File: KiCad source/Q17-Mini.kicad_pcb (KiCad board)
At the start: 2 copper layers, 95 x 75 mm, 85 parts, among them J1 Input, Q1 FQP3N30, Q10 KSA992, Q11 BS250P, Q12 BD139, Q13 FQP3N30, Q14 IRF9610, Q15 FQA46N15, Q16 FQA36P15, Q2 KSA992, Q3 KSC1845, Q4 FQP3P20, Q5 FQP3P20, Q6 FQP3N30, Q7 KSC1845, Q8 2N7000, Q9 BS250P, U1 OPA1641

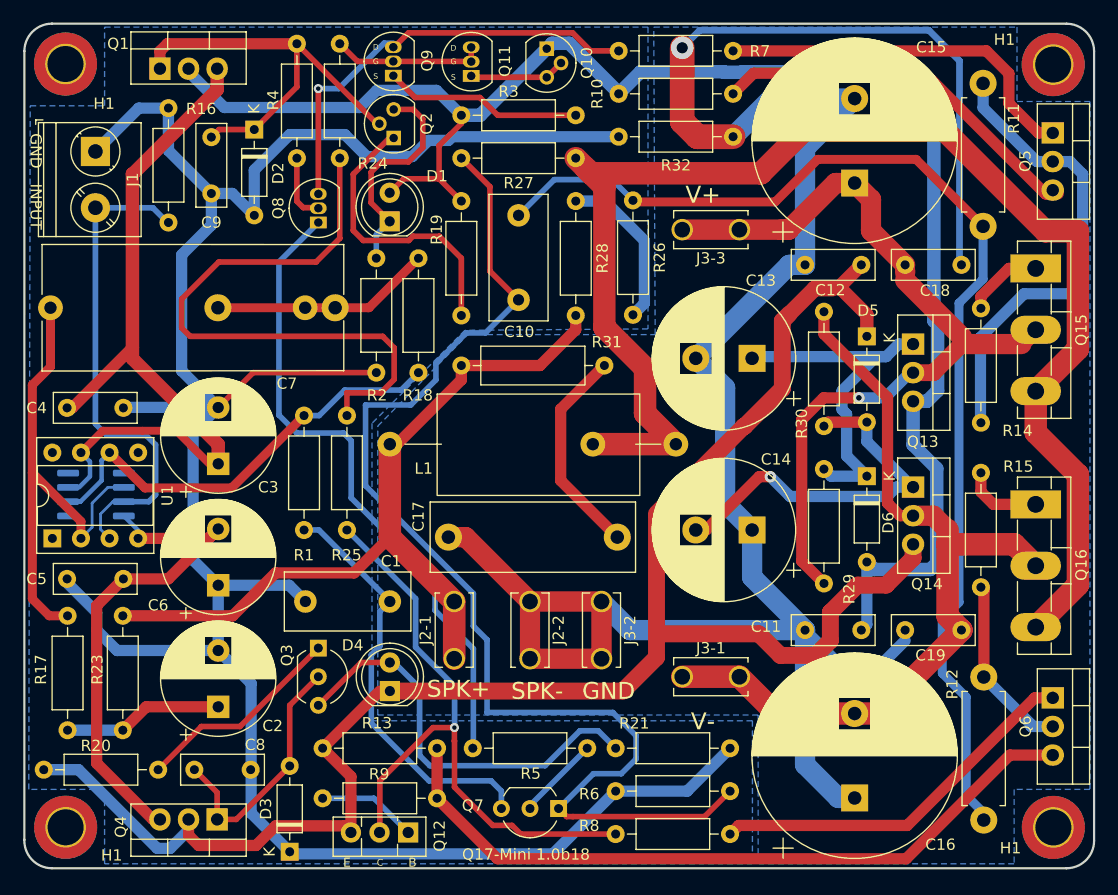
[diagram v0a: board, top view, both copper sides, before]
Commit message: PCB version 1.0b19
More mods on ground plane.
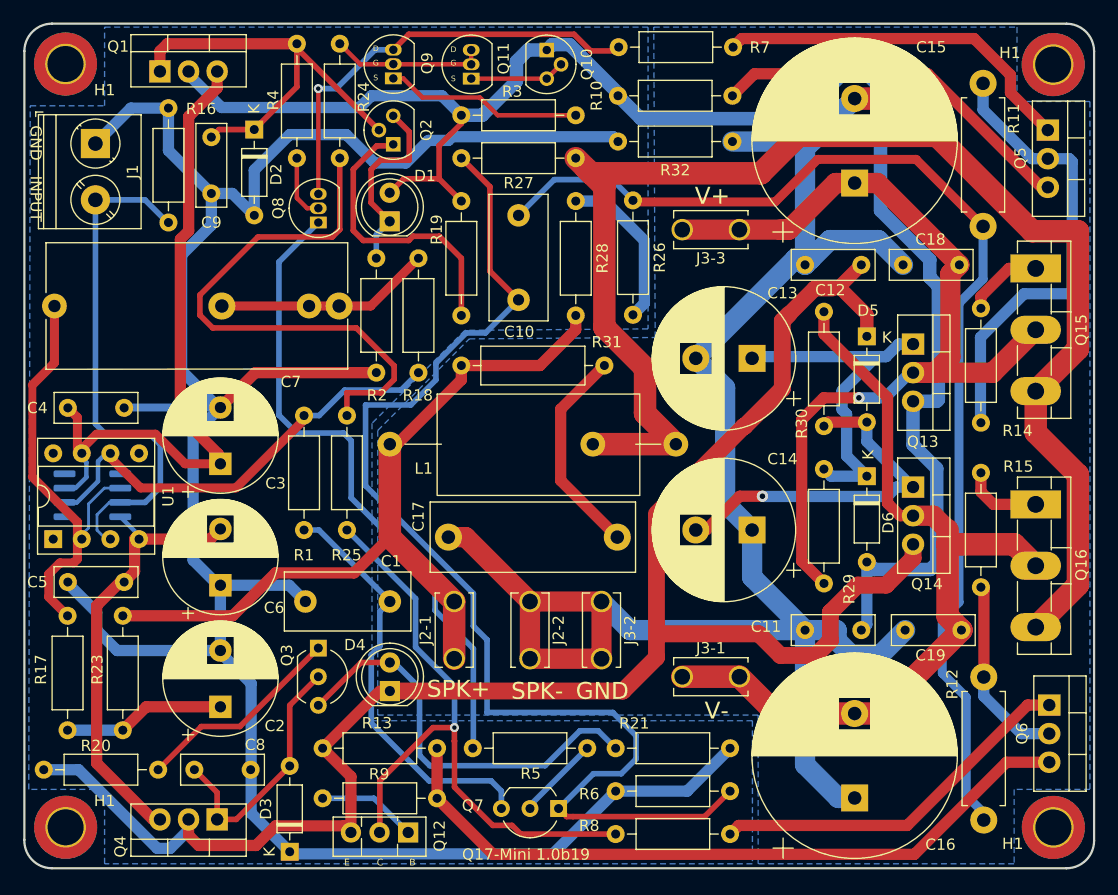
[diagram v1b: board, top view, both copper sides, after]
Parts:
- moved C18 5.19 mm to (177.8, 76.5), turned to 0 degrees
- moved Q6 0.71 mm to (190.8, 115.6)
- moved J1 0.70 mm to (106.1, 65.7)
- moved Q2 0.57 mm to (132.6, 65.8)
- moved Q5 0.51 mm to (190.7, 64.5)
- moved R32 0.43 mm to (152.5, 65.5)
- moved C7 0.38 mm to (102.4, 80.1)
- moved R7 0.33 mm to (152.6, 57.1)
- moved U1 0.32 mm to (105.9, 96.9)
- moved C5 0.29 mm to (103.7, 104.6)
- moved Q1 0.25 mm to (111.9, 59.3)
- moved Q11 0.24 mm to (139.5, 59.9)
- moved Q9 0.24 mm to (132.6, 59.9)
- moved C2 0.19 mm to (117.2, 115.7)
- moved C3 0.19 mm to (117.2, 94.2)
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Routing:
- net GNDPWR: track 207.5 -> 168.3 mm
- net Net-(C3-Pad1): track 67.4 -> 60.3 mm
- net Net-(C15-Pad1): track 75.4 -> 82.4 mm
- net Net-(C5-Pad2): track 45.3 -> 39.7 mm
- net Net-(C7-Pad1): track 44.8 -> 39.4 mm
- net Net-(R24-Pad2): track 55.1 -> 50.0 mm
- net Net-(D1-Pad1): track 19.8 -> 17.3 mm
- net Net-(J1-Pad2): track 43.8 -> 45.6 mm
- net Net-(C14-Pad2): track 33.7 -> 32.3 mm
- net Net-(Q5-Pad3): track 34.1 -> 33.0 mm
- net Net-(Q6-Pad3): track 65.2 -> 64.3 mm
- net Net-(Q6-Pad2): track 16.1 -> 17.0 mm
- net Net-(Q6-Pad1): track 33.8 -> 33.1 mm
- net Net-(C11-Pad2): track 146.6 -> 147.1 mm
- net Net-(Q5-Pad2): track 41.6 -> 41.1 mm
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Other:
- board text added: "Q17-Mini 1.0b19"
- board text added: "QUAD405 Audiophile Tiberiu Vicol PCB Design by Stef PROTO RELEASE 2021"
- board text removed: "2022"
- board text removed: "Q17-Mini 1.0b18"
- board text removed: "QUAD405 Audiophile Tiberiu Vicol PCB Design by Stef PROTO RELEASE"

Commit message: PCB 1.0b20
- New Faston PAD footprint + 3D view.
- Removed old GND track.
- More track optimisation.
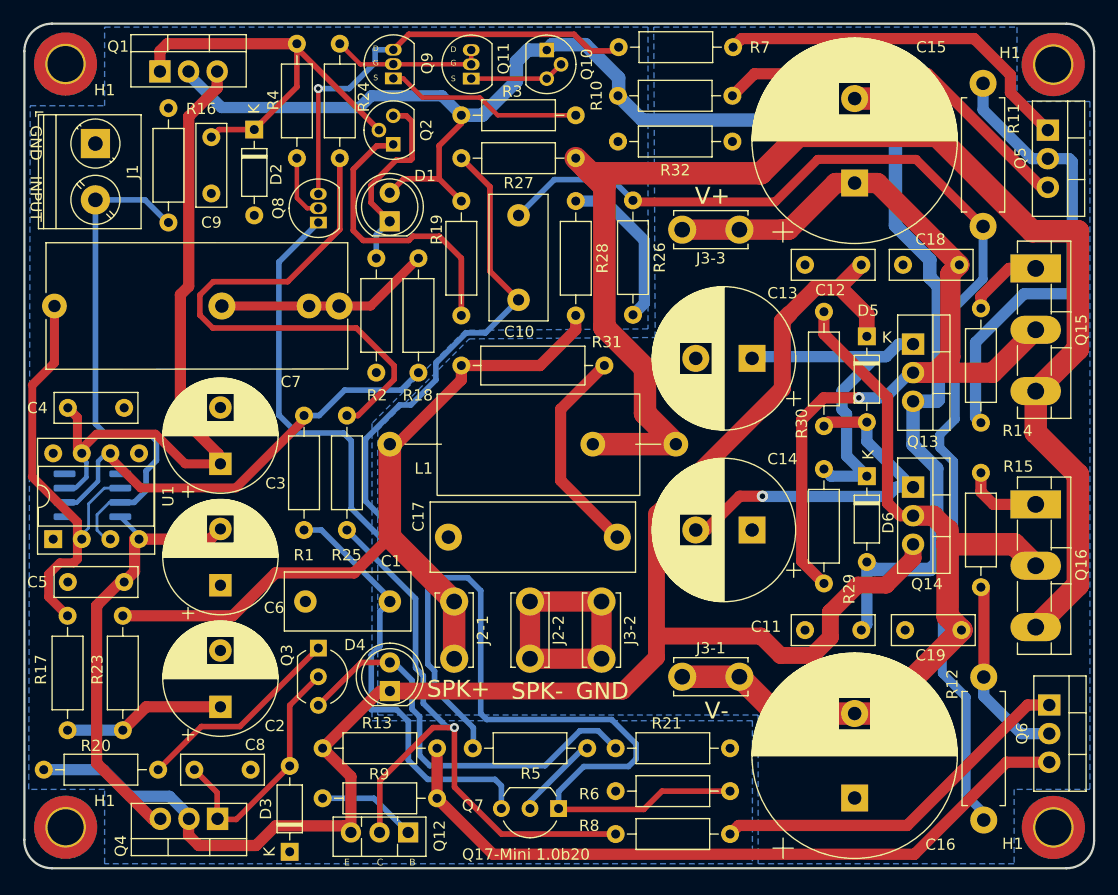
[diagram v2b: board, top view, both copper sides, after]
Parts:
- moved Q4 0.07 mm to (117.0, 125.7)
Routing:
- net GND: track 220.3 -> 0.39 mm
- net GNDPWR: track 168.3 -> 29.2 mm
- net Net-(C11-Pad2): track 147.1 -> 149.7 mm
- net Net-(C1-Pad1): track 37.3 -> 39.0 mm
- net Net-(C12-Pad2): track 152.8 -> 151.5 mm
- net Net-(R24-Pad2): track 50.0 -> 48.8 mm
- net Net-(C10-Pad1): track 103.4 -> 104.4 mm
- net Net-(J1-Pad2): track 45.6 -> 44.7 mm
- net Net-(Q8-Pad3): track 38.6 -> 39.3 mm
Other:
- board text added: "Q17-Mini 1.0b20"
- board text removed: "Q17-Mini 1.0b19"

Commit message: PCB 1.0b21
- New footprint for Silver Mica capacitors.
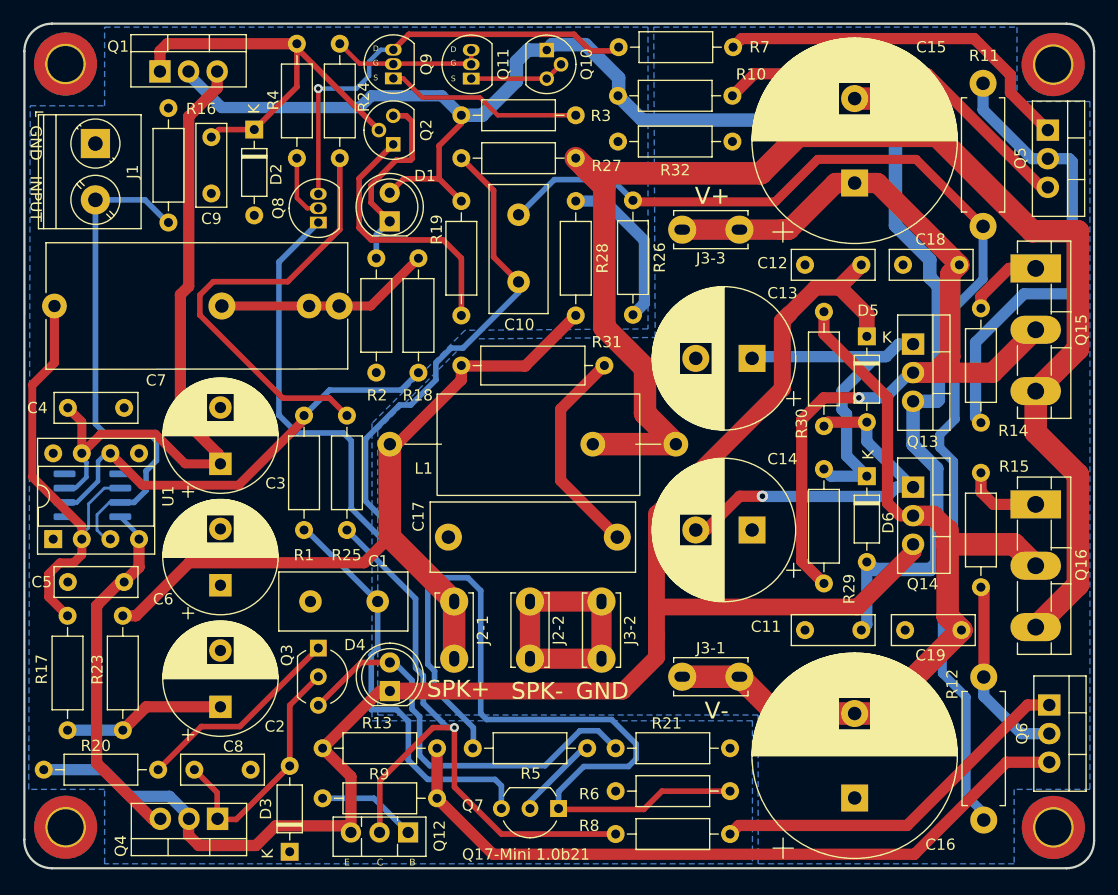
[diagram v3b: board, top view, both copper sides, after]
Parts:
- C1, C10: footprint Capacitor_THT:C_Disc_D11.0mm_W5.0mm_P7.50mm -> Silver_Mica:C_Mica_L11.4mm_W4.3mm_H9.1_P5.9mm
- moved C1 1.14 mm to (131.1, 106.4)
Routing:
- net Net-(R24-Pad2): track 48.8 -> 39.7 mm
- net Net-(C5-Pad2): track 39.7 -> 31.9 mm
- net Net-(C12-Pad2): track 151.5 -> 147.4 mm
- net Net-(Q2-Pad1): track 25.9 -> 23.9 mm
- net Net-(C1-Pad1): track 39.0 -> 37.4 mm
- net Net-(J2-Pad1): track 70.8 -> 70.0 mm
- net Net-(R1-Pad1): track 40.0 -> 39.4 mm
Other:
- board text added: "Q17-Mini 1.0b21"
- board text removed: "Q17-Mini 1.0b20"

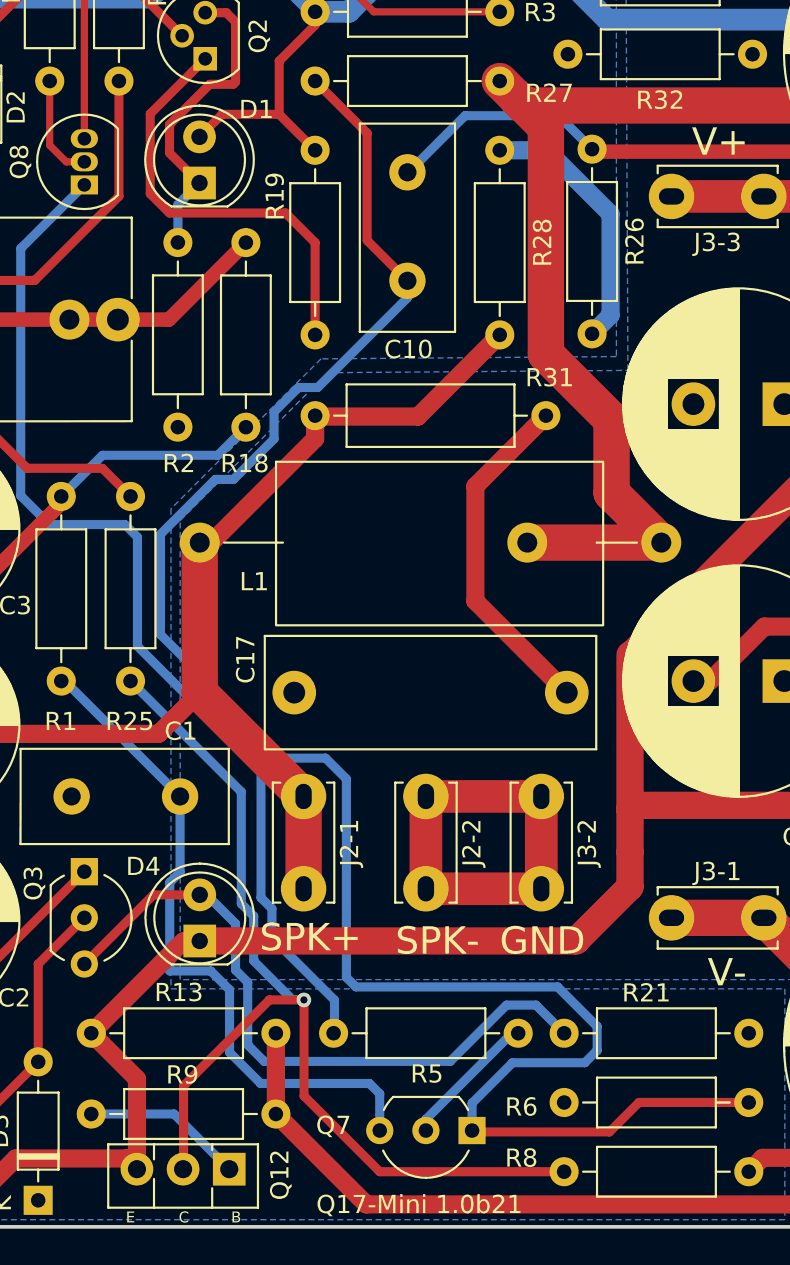
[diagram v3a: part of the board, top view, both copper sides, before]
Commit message: PCB v1.0b21
- New footprint for final 1.2uH air inductor.
- Silver Mica capacitors with right footprint and 3D size.
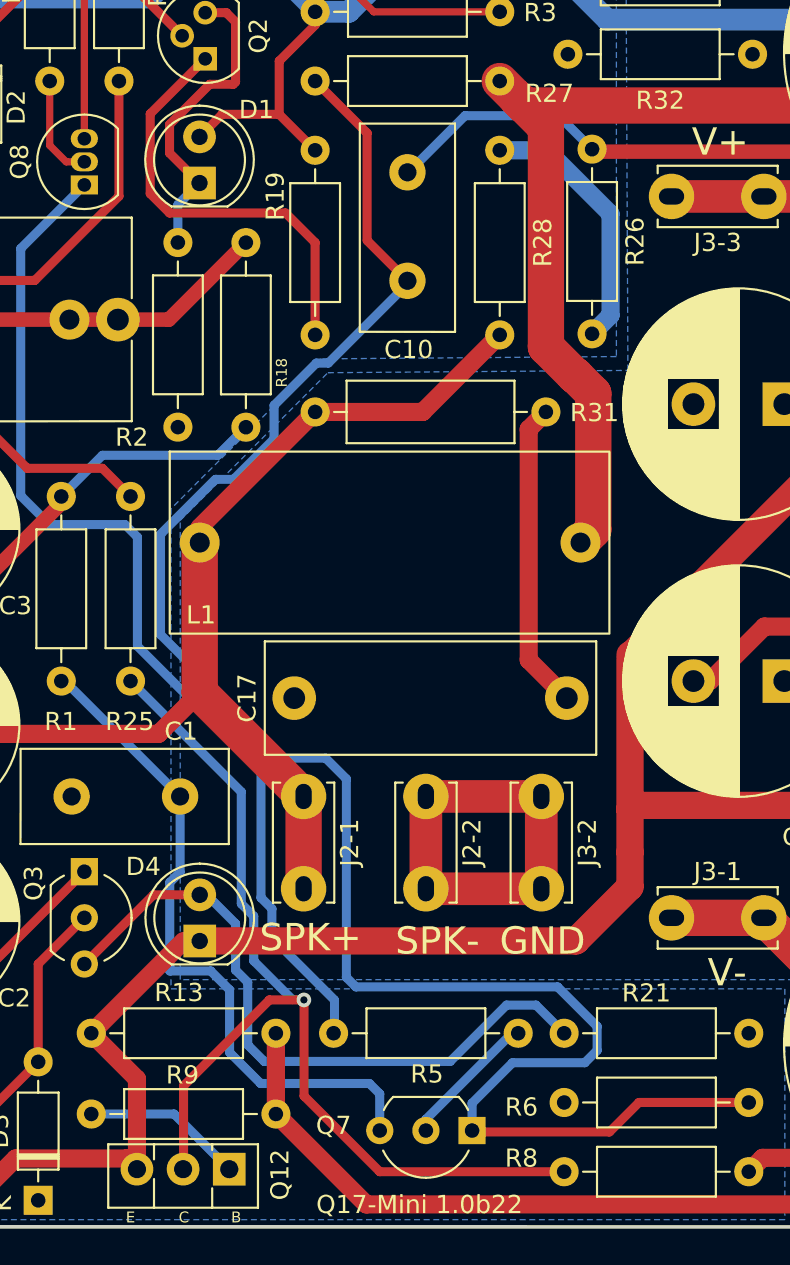
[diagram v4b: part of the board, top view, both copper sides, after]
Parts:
- L1: footprint Inductor_THT:L_Axial_L16.0mm_D7.5mm_P25.40mm_Horizontal_Fastron_XHBCC -> Inductor_THT:L_Axial_L22mm_D10mm_P21mm_Horizontal_Q17_Mini
- moved C17 0.30 mm to (152.5, 101.0)
- moved R31 0.21 mm to (138.6, 85.2)
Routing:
- net Net-(L1-Pad2): track 126.3 -> 117.7 mm
- net Net-(C17-Pad1): track 18.9 -> 17.0 mm
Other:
- board text added: "Q17-Mini 1.0b22"
- board text removed: "Q17-Mini 1.0b21"
